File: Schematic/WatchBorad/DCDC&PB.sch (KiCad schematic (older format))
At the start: 27 parts, among them M1 Motor_DC, SW3 SW_Push, SW4 SW_Push, SW5 SW_Push, U10 TPS62740DSST, U9 MAX809S

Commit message: Fixed board's proposals. Fixed testpoints' footprint. Fixed DRC violations. Added +5V testpoint
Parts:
- TP13, TP14, TP15: footprint Measurement_Points:Measurement_Point_Round-SMD-Pad_Small -> TestPoint:TestPoint_Pad_D2.0mm
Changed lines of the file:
@@
 F 0 "TP15" H 7083 1722 50  0000 L CNN
 F 1 "TestPoint" H 7083 1677 50  0001 L CNN
-F 2 "Measurement_Points:Measurement_Point_Round-SMD-Pad_Small" H 7225 1650 50  0001 C CNN
+F 2 "TestPoint:TestPoint_Pad_D2.0mm" H 7225 1650 50  0001 C CNN
 F 3 "~" H 7225 1650 50  0001 C CNN
 	1    7025 1650
@@
 F 0 "TP14" H 2958 2572 50  0000 L CNN
 F 1 "TestPoint" H 2958 2527 50  0001 L CNN
-F 2 "Measurement_Points:Measurement_Point_Round-SMD-Pad_Small" H 3100 2500 50  0001 C CNN
+F 2 "TestPoint:TestPoint_Pad_D2.0mm" H 3100 2500 50  0001 C CNN
 F 3 "~" H 3100 2500 50  0001 C CNN
 	1    2900 2500
@@
 F 0 "TP13" H 1933 5247 50  0000 L CNN
 F 1 "TestPoint" H 1933 5202 50  0001 L CNN
-F 2 "Measurement_Points:Measurement_Point_Round-SMD-Pad_Small" H 2075 5175 50  0001 C CNN
+F 2 "TestPoint:TestPoint_Pad_D2.0mm" H 2075 5175 50  0001 C CNN
 F 3 "~" H 2075 5175 50  0001 C CNN
 	1    1875 5175

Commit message: Added new DCDC and radio antenna from Rulepas [SCHECMATIC]
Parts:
- removed U10: TPS62740DSST, Housings_SON:WSON-12-1EP_3x2mm_Pitch0.5mm, symbol WatchBorad-rescue:TPS62740DSST-DCDC_Local-WatchBorad-rescue-WatchBorad-rescue
- added C?: 100 nF, Capacitor_SMD:C_0603_1608Metric, symbol Device:C
- added C?: 10 uF, Capacitor_SMD:C_0603_1608Metric, symbol Device:C
- added C?: 4.7 pF, Capacitor_SMD:C_0603_1608Metric, symbol Device:C
- added C?: 330 pF, Capacitor_SMD:C_0603_1608Metric, symbol Device:C
- added C?: 47 pF, Capacitor_SMD:C_0603_1608Metric, symbol Device:C
- added R?: 33.2k, Resistor_SMD:R_0603_1608Metric, symbol Device:R
- added R? (x2): 200k, Resistor_SMD:R_0603_1608Metric, symbol Device:R
- added R?: 340k, Resistor_SMD:R_0603_1608Metric, symbol Device:R
- added R?: 107k, Resistor_SMD:R_0603_1608Metric, symbol Device:R
- added R?: 6.49k, Resistor_SMD:R_0603_1608Metric, symbol Device:R
- added U?: LTC3533, Housings_DFN_QFN:DFN-14-1EP_3x4mm_Pitch0.5mm, symbol WatchBorad-rescue:LTC3533-DCDC_Local
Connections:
- net labels added: COMP, DCDC_FB, L_SW_1, L_SW_2
- net labels removed: L_SW_0
- wire segments 98 -> 140
- no-connect marks 2 -> 0
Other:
- note added: "If V_OUT_MUX below 2.93V than DC/DC is off"
- note removed: "Connect this pin(5) directly \nto the output capacitor\n with a short trace"
- note removed: "If V_OUT_MUX below 3.0V than DC/DC is off"
- note removed: "LOAD(out)\nis disabled"
- moved on the sheet: C35, L1, TP15

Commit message: Added schematic files annotations [SCHEMATIC]
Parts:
- U12: renamed from U?; footprint Housings_DFN_QFN:DFN-14-1EP_3x4mm_Pitch0.5mm -> Package_DFN_QFN:DFN-14-1EP_3x4mm_P0.5mm_EP1.7x3.3mm
- gave numbers to parts that had none: 11
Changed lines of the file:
@@
 U 1 1 61909063
 P 4775 2275
-F 0 "U?" H 4775 2825 50  0000 C CNN
+AR Path="/61909063" Ref="U?"  Part="1"
+AR Path="/5F988DA5/61909063" Ref="U12"  Part="1"
+F 0 "U12" H 4775 2825 50  0000 C CNN
 F 1 "LTC3533" H 4775 2300 50  0000 C CNN
-F 2 "Housings_DFN_QFN:DFN-14-1EP_3x4mm_Pitch0.5mm" H 4775 2375 50  0001 C CNN
+F 2 "Package_DFN_QFN:DFN-14-1EP_3x4mm_P0.5mm_EP1.7x3.3mm" H 4775 2375 50  0001 C CNN
 F 3 "https://datasheet.lcsc.com/lcsc/1912111437_Analog-Devices-LTC3533EDE-TRPBF_C461524.pdf" H 4775 2375 50  0001 C CNN
 	1    4775 2275
@@
 AR Path="/5EA4867C/6191DAA1" Ref="R?"  Part="1"
 AR Path="/5F7F86D0/6191DAA1" Ref="R?"  Part="1"
-AR Path="/5F988DA5/6191DAA1" Ref="R?"  Part="1"
-F 0 "R?" H 4220 2796 50  0000 L CNN
+AR Path="/5F988DA5/6191DAA1" Ref="R3"  Part="1"
+F 0 "R3" H 4220 2796 50  0000 L CNN
 F 1 "33.2k" H 4220 2705 50  0000 L CNN
 F 2 "Resistor_SMD:R_0603_1608Metric" V 4080 2750 50  0001 C CNN
@@
 AR Path="/5EA4867C/6193FCF4" Ref="R?"  Part="1"
 AR Path="/5F7F86D0/6193FCF4" Ref="R?"  Part="1"
-AR Path="/5F988DA5/6193FCF4" Ref="R?"  Part="1"
-F 0 "R?" H 5470 2771 50  0000 L CNN
+AR Path="/5F988DA5/6193FCF4" Ref="R19"  Part="1"
+F 0 "R19" H 5470 2771 50  0000 L CNN
 F 1 "200k" H 5470 2680 50  0000 L CNN
 F 2 "Resistor_SMD:R_0603_1608Metric" V 5330 2725 50  0001 C CNN
@@
 AR Path="/5E9C1C3A/619482E5" Ref="C?"  Part="1"
 AR Path="/5F7F86D0/619482E5" Ref="C?"  Part="1"
-AR Path="/5F988DA5/619482E5" Ref="C?"  Part="1"
-F 0 "C?" H 5775 2800 50  0000 L CNN
+AR Path="/5F988DA5/619482E5" Ref="C8"  Part="1"
+F 0 "C8" H 5775 2800 50  0000 L CNN
 F 1 "100 nF" H 5775 2625 50  0000 L CNN
 F 2 "Capacitor_SMD:C_0603_1608Metric" H 5788 2575 50  0001 C CNN
@@
 AR Path="/5E9C1C3A/61961E73" Ref="C?"  Part="1"
 AR Path="/5F7F86D0/61961E73" Ref="C?"  Part="1"
-AR Path="/5F988DA5/61961E73" Ref="C?"  Part="1"
-F 0 "C?" H 7600 1975 50  0000 L CNN
+AR Path="/5F988DA5/61961E73" Ref="C40"  Part="1"
+F 0 "C40" H 7600 1975 50  0000 L CNN
 F 1 "10 uF" H 7575 1900 50  0000 L CNN
 F 2 "Capacitor_SMD:C_0603_1608Metric" H 7488 1775 50  0001 C CNN
@@
 AR Path="/5EA4867C/619772C6" Ref="R?"  Part="1"
 AR Path="/5F7F86D0/619772C6" Ref="R?"  Part="1"
-AR Path="/5F988DA5/619772C6" Ref="R?"  Part="1"
-F 0 "R?" H 6845 1971 50  0000 L CNN
+AR Path="/5F988DA5/619772C6" Ref="R25"  Part="1"
+F 0 "R25" H 6845 1971 50  0000 L CNN
 F 1 "340k" H 6845 1880 50  0000 L CNN
 F 2 "Resistor_SMD:R_0603_1608Metric" V 6705 1925 50  0001 C CNN
@@
 AR Path="/5EA4867C/6197810D" Ref="R?"  Part="1"
 AR Path="/5F7F86D0/6197810D" Ref="R?"  Part="1"
-AR Path="/5F988DA5/6197810D" Ref="R?"  Part="1"
-F 0 "R?" H 7170 2771 50  0000 L CNN
+AR Path="/5F988DA5/6197810D" Ref="R35"  Part="1"
+F 0 "R35" H 7170 2771 50  0000 L CNN
 F 1 "200k" H 7170 2680 50  0000 L CNN
 F 2 "Resistor_SMD:R_0603_1608Metric" V 7030 2725 50  0001 C CNN
@@
 AR Path="/5EA4867C/61996769" Ref="R?"  Part="1"
 AR Path="/5F7F86D0/61996769" Ref="R?"  Part="1"
-AR Path="/5F988DA5/61996769" Ref="R?"  Part="1"
-F 0 "R?" V 6325 2125 50  0000 L CNN
+AR Path="/5F988DA5/61996769" Ref="R22"  Part="1"
+F 0 "R22" V 6325 2125 50  0000 L CNN
 F 1 "107k" V 6375 2275 50  0000 L CNN
 F 2 "Resistor_SMD:R_0603_1608Metric" V 6305 2375 50  0001 C CNN
@@
 AR Path="/5E9C1C3A/619CAFA1" Ref="C?"  Part="1"
 AR Path="/5F7F86D0/619CAFA1" Ref="C?"  Part="1"
-AR Path="/5F988DA5/619CAFA1" Ref="C?"  Part="1"
-F 0 "C?" V 6325 2375 50  0000 L CNN
+AR Path="/5F988DA5/619CAFA1" Ref="C11"  Part="1"
+F 0 "C11" V 6325 2375 50  0000 L CNN
 F 1 "4.7 pF" V 6500 2475 50  0000 L CNN
 F 2 "Capacitor_SMD:C_0603_1608Metric" H 6413 2450 50  0001 C CNN
@@
 AR Path="/5E9C1C3A/619CBCE2" Ref="C?"  Part="1"
 AR Path="/5F7F86D0/619CBCE2" Ref="C?"  Part="1"
-AR Path="/5F988DA5/619CBCE2" Ref="C?"  Part="1"
-F 0 "C?" V 6775 2150 50  0000 L CNN
+AR Path="/5F988DA5/619CBCE2" Ref="C17"  Part="1"
+F 0 "C17" V 6775 2150 50  0000 L CNN
 F 1 "330 pF" V 6950 2250 50  0000 L CNN
 F 2 "Capacitor_SMD:C_0603_1608Metric" H 6863 2225 50  0001 C CNN
@@
 AR Path="/5EA4867C/619E85E1" Ref="R?"  Part="1"
 AR Path="/5F7F86D0/619E85E1" Ref="R?"  Part="1"
-AR Path="/5F988DA5/619E85E1" Ref="R?"  Part="1"
-F 0 "R?" H 7170 1971 50  0000 L CNN
+AR Path="/5F988DA5/619E85E1" Ref="R34"  Part="1"
+F 0 "R34" H 7170 1971 50  0000 L CNN
 F 1 "6.49k" H 7170 1880 50  0000 L CNN
 F 2 "Resistor_SMD:R_0603_1608Metric" V 7030 1925 50  0001 C CNN
@@
 AR Path="/5E9C1C3A/619ED8AC" Ref="C?"  Part="1"
 AR Path="/5F7F86D0/619ED8AC" Ref="C?"  Part="1"
-AR Path="/5F988DA5/619ED8AC" Ref="C?"  Part="1"
-F 0 "C?" V 6900 2400 50  0000 L CNN
+AR Path="/5F988DA5/619ED8AC" Ref="C39"  Part="1"
+F 0 "C39" V 6900 2400 50  0000 L CNN
 F 1 "47 pF" V 7000 2400 50  0000 L CNN
 F 2 "Capacitor_SMD:C_0603_1608Metric" H 6988 2025 50  0001 C CNN

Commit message: Added LDO instead of DC-DC. Added board routing accroding to the new peripheral changes [SCHEMATIC]
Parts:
- removed C11: 4.7 pF, Capacitor_SMD:C_0603_1608Metric, symbol Device:C
- removed C17: 330 pF, Capacitor_SMD:C_0603_1608Metric, symbol Device:C
- removed C35: 10 uF, Capacitor_SMD:C_0603_1608Metric, symbol Device:C
- removed C39: 47 pF, Capacitor_SMD:C_0603_1608Metric, symbol Device:C
- removed C8: 100 nF, Capacitor_SMD:C_0603_1608Metric, symbol Device:C
- removed L1: 2.2 uH 13.75 mOHM 1.2 A, Inductors_SMD:L_0805_HandSoldering, symbol pspice:INDUCTOR
- removed R22: 107k, Resistor_SMD:R_0603_1608Metric, symbol Device:R
- removed R25: 340k, Resistor_SMD:R_0603_1608Metric, symbol Device:R
- removed R34: 6.49k, Resistor_SMD:R_0603_1608Metric, symbol Device:R
- removed R35: 200k, Resistor_SMD:R_0603_1608Metric, symbol Device:R
- removed U12: LTC3533, Package_DFN_QFN:DFN-14-1EP_3x4mm_P0.5mm_EP1.7x3.3mm, symbol WatchBorad-rescue:LTC3533-DCDC_Local
- added U12: TPS73501DRBR, TPS73501DRBR:TPS73501DRBR, symbol TPS73501DRBR:TPS73501DRBR
- R19: value 200k -> 220
- R3: value 33.2k -> 330
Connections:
- net labels added: LDO_RDIV
- net labels removed: COMP, DCDC_FB, L_SW_1, L_SW_2
- wire segments 140 -> 89
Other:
- note added: "LDO 3.0V\n\n"
- note added: "Vout = 3.0V\n"
- note added: "Vout=(R1+R2)/R2 * 1.208\n"
- note removed: "DCDC converter 3.3V\n\n"
- note removed: "Vout = 3.3V\n"
- moved on the sheet: C40, TP15

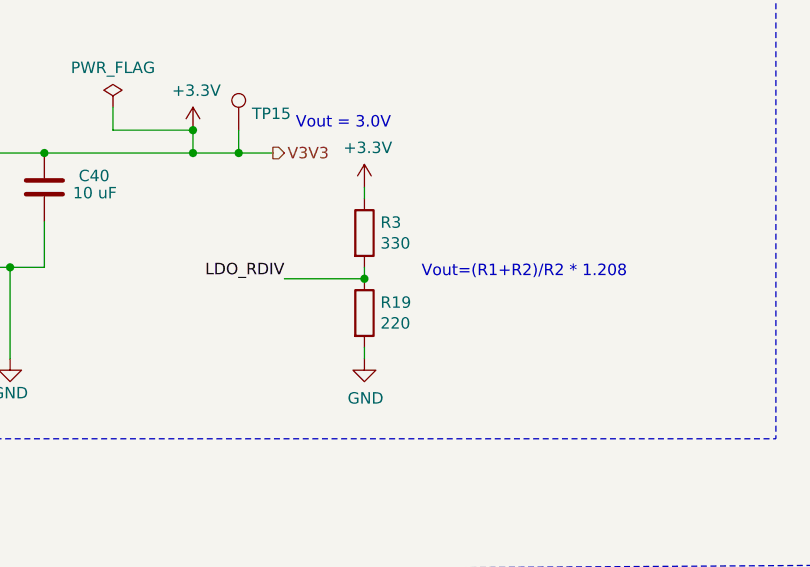
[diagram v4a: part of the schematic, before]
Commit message: Adjusted LDO resisors [SCHEMATIC]
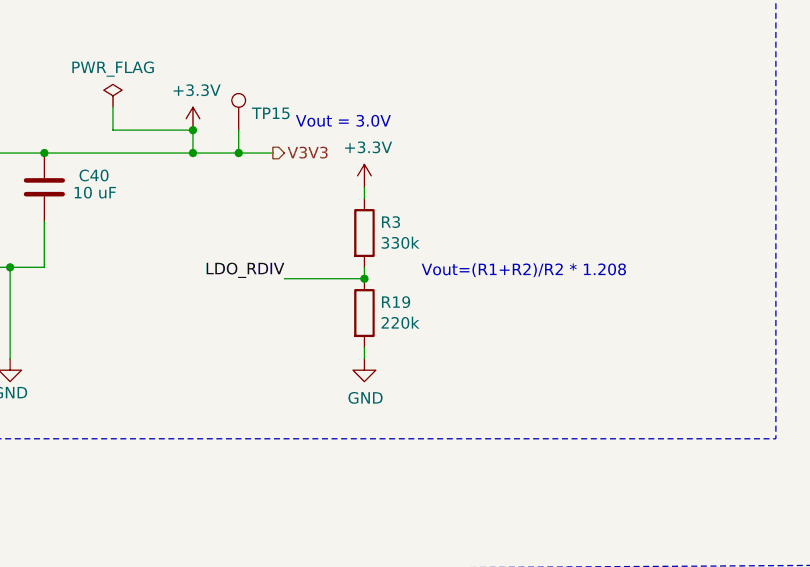
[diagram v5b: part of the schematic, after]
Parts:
- R19: value 220 -> 220k
- R3: value 330 -> 330k
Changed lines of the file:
@@
 P 7300 2800
 F 0 "R19" H 7370 2846 50  0000 L CNN
-F 1 "220" H 7370 2755 50  0000 L CNN
+F 1 "220k" H 7370 2755 50  0000 L CNN
 F 2 "Resistor_SMD:R_0603_1608Metric" V 7230 2800 50  0001 C CNN
 F 3 "~" H 7300 2800 50  0001 C CNN
@@
 P 7300 2450
 F 0 "R3" H 7370 2496 50  0000 L CNN
-F 1 "330" H 7370 2405 50  0000 L CNN
+F 1 "330k" H 7370 2405 50  0000 L CNN
 F 2 "Resistor_SMD:R_0603_1608Metric" V 7230 2450 50  0001 C CNN
 F 3 "~" H 7300 2450 50  0001 C CNN

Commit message: Added missed components to the symbol lists [SCHEMATIC]
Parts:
- C32, C34, C36, C37, C38: lcsc (none) -> https://lcsc.com/product-detail/Multilayer-Ceramic-Capacito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
- M1: lcsc (none) -> https://www.aliexpress.com/item/32844746278.html?spm=a2g0o.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
- U12: lcsc (none) -> https://lcsc.com/product-detail/Linear-Voltage-Regulators-L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
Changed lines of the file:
@@
 F 2 "Capacitor_SMD:C_0603_1608Metric" H 2038 2350 50  0001 C CNN
 F 3 "~" H 2000 2500 50  0001 C CNN
+F 4 "https://lcsc.com/product-detail/Multilayer-Ceramic-Capacitors-MLCC-SMD-SMT_YAGEO-CC0603KRX7R9BB104_C14663.html" H 2000 2500 50  0001 C CNN "lcsc"
 	1    2000 2500
 	1    0    0    -1
@@
 F 2 "LocalFootprints:VibrationMorot4x4x11" H 2975 4460 50  0001 C CNN
 F 3 "https://www.aliexpress.com/item/32844746278.html?spm=a2g0o.productlist.0.0.24ef228a6Cfn5S&algo_pvid=3165a7c1-ba73-4c2c-bb27-6dacea1bed25&algo_expid=3165a7c1-ba73-4c2c-bb27-6dacea1bed25-0&btsid=0b8b15c915866028623212205ec781&ws_ab_test=searchweb0_0,searchweb201602_,searchweb201603_" H 2975 4460 50  0001 C CNN
+F 4 "https://www.aliexpress.com/item/32844746278.html?spm=a2g0o.productlist.0.0.24ef228a6Cfn5S&algo_pvid=3165a7c1-ba73-4c2c-bb27-6dacea1bed25&algo_expid=3165a7c1-ba73-4c2c-bb27-6dacea1bed25-0&btsid=0b8b15c915866028623212205ec781&ws_ab_test=searchweb0_0,searchweb201602_,searchweb201603_" H 2975 4550 50  0001 C CNN "lcsc"
 	1    2975 4550
 	1    0    0    -1
@@
 F 2 "Capacitor_SMD:C_0603_1608Metric" H 3438 4475 50  0001 C CNN
 F 3 "~" H 3400 4625 50  0001 C CNN
+F 4 "https://lcsc.com/product-detail/Multilayer-Ceramic-Capacitors-MLCC-SMD-SMT_Samsung-Electro-Mechanics-CL10B104KO8NNNC_C66501.html" H 3400 4625 50  0001 C CNN "lcsc"
 	1    3400 4625
 	1    0    0    -1
@@
 F 2 "Capacitor_SMD:C_0603_1608Metric" H 7763 5350 50  0001 C CNN
 F 3 "~" H 7725 5500 50  0001 C CNN
+F 4 "https://lcsc.com/product-detail/Multilayer-Ceramic-Capacitors-MLCC-SMD-SMT_YAGEO-CC0603KRX7R9BB104_C14663.html" H 7725 5500 50  0001 C CNN "lcsc"
 	1    7725 5500
 	1    0    0    -1
@@
 F 2 "Capacitor_SMD:C_0603_1608Metric" H 8463 5350 50  0001 C CNN
 F 3 "~" H 8425 5500 50  0001 C CNN
+F 4 "https://lcsc.com/product-detail/Multilayer-Ceramic-Capacitors-MLCC-SMD-SMT_YAGEO-CC0603KRX7R9BB104_C14663.html" H 8425 5500 50  0001 C CNN "lcsc"
 	1    8425 5500
 	1    0    0    -1
@@
 F 2 "Capacitor_SMD:C_0603_1608Metric" H 9188 5350 50  0001 C CNN
 F 3 "~" H 9150 5500 50  0001 C CNN
+F 4 "https://lcsc.com/product-detail/Multilayer-Ceramic-Capacitors-MLCC-SMD-SMT_YAGEO-CC0603KRX7R9BB104_C14663.html" H 9150 5500 50  0001 C CNN "lcsc"
 	1    9150 5500
 	1    0    0    -1
@@
 F 2 "TPS73501DRBR:TPS73501DRBR" H 4950 2400 50  0001 L BNN
 F 3 "" H 4950 2400 50  0001 L BNN
+F 4 "https://lcsc.com/product-detail/Linear-Voltage-Regulators-LDO_Texas-Instruments-TPS73501DRBR_C130077.html" H 4950 2400 50  0001 C CNN "lcsc"
 	1    4950 2400
 	1    0    0    -1

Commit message: Added missed resistors to the lcsc [SCHEMATIC][BOM]
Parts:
- R19, R26, R27, R28, R29, R3, R30, R31, R32, R33: lcsc (none) -> https://www.lcsc.com/product-detail/Chip-Resistor-Surface-M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
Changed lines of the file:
@@
 F 2 "Resistor_SMD:R_0603_1608Metric" V 7905 5500 50  0001 C CNN
 F 3 "~" H 7975 5500 50  0001 C CNN
+F 4 "https://www.lcsc.com/product-detail/Chip-Resistor-Surface-Mount_YAGEO-RC0603FR-0710KL_C98220.html" H 7975 5500 50  0001 C CNN "lcsc"
 	1    7975 5500
 	1    0    0    -1
@@
 F 2 "Resistor_SMD:R_0603_1608Metric" V 8605 5500 50  0001 C CNN
 F 3 "~" H 8675 5500 50  0001 C CNN
+F 4 "https://www.lcsc.com/product-detail/Chip-Resistor-Surface-Mount_YAGEO-RC0603FR-0710KL_C98220.html" H 8675 5500 50  0001 C CNN "lcsc"
 	1    8675 5500
 	1    0    0    -1
@@
 F 2 "Resistor_SMD:R_0603_1608Metric" V 9330 5500 50  0001 C CNN
 F 3 "~" H 9400 5500 50  0001 C CNN
+F 4 "https://www.lcsc.com/product-detail/Chip-Resistor-Surface-Mount_YAGEO-RC0603FR-0710KL_C98220.html" H 9400 5500 50  0001 C CNN "lcsc"
 	1    9400 5500
 	1    0    0    -1
@@
 F 2 "Resistor_SMD:R_0603_1608Metric" V 2605 5500 50  0001 C CNN
 F 3 "~" H 2675 5500 50  0001 C CNN
+F 4 "https://www.lcsc.com/product-detail/Chip-Resistor-Surface-Mount_YAGEO-RC0603FR-0710KL_C98220.html" H 2675 5500 50  0001 C CNN "lcsc"
 	1    2675 5500
 	1    0    0    -1
@@
 F 2 "Resistor_SMD:R_0603_1608Metric" V 2330 5175 50  0001 C CNN
 F 3 "https://lcsc.com/product-detail/Others_Viking-Tech-ARG03FTC3300_C217969.html" H 2400 5175 50  0001 C CNN
+F 4 "https://www.lcsc.com/product-detail/Chip-Resistor-Surface-Mount_Walsin-Tech-Corp-WR06X331JTL_C384242.html" H 2400 5175 50  0001 C CNN "lcsc"
 	1    2400 5175
 	0    1    1    0
@@
 F 2 "Resistor_SMD:R_0603_1608Metric" V 7030 5050 50  0001 C CNN
 F 3 "https://lcsc.com/product-detail/Others_Viking-Tech-ARG03FTC3300_C217969.html" H 7100 5050 50  0001 C CNN
+F 4 "https://www.lcsc.com/product-detail/Chip-Resistor-Surface-Mount_Walsin-Tech-Corp-WR06X331JTL_C384242.html" H 7100 5050 50  0001 C CNN "lcsc"
 	1    7100 5050
 	0    1    1    0
@@
 F 2 "Resistor_SMD:R_0603_1608Metric" V 7030 5150 50  0001 C CNN
 F 3 "https://lcsc.com/product-detail/Others_Viking-Tech-ARG03FTC3300_C217969.html" H 7100 5150 50  0001 C CNN
+F 4 "https://www.lcsc.com/product-detail/Chip-Resistor-Surface-Mount_Walsin-Tech-Corp-WR06X331JTL_C384242.html" H 7100 5150 50  0001 C CNN "lcsc"
 	1    7100 5150
 	0    1    1    0
@@
 F 2 "Resistor_SMD:R_0603_1608Metric" V 7030 5250 50  0001 C CNN
 F 3 "https://lcsc.com/product-detail/Others_Viking-Tech-ARG03FTC3300_C217969.html" H 7100 5250 50  0001 C CNN
+F 4 "https://www.lcsc.com/product-detail/Chip-Resistor-Surface-Mount_Walsin-Tech-Corp-WR06X331JTL_C384242.html" H 7100 5250 50  0001 C CNN "lcsc"
 	1    7100 5250
 	0    1    1    0
@@
 F 2 "Resistor_SMD:R_0603_1608Metric" V 7230 2800 50  0001 C CNN
 F 3 "~" H 7300 2800 50  0001 C CNN
+F 4 "https://www.lcsc.com/product-detail/Chip-Resistor-Surface-Mount_FH-Guangdong-Fenghua-Advanced-Tech-RS-03K224JT_C118377.html" H 7300 2800 50  0001 C CNN "lcsc"
 	1    7300 2800
 	1    0    0    -1
@@
 F 2 "Resistor_SMD:R_0603_1608Metric" V 7230 2450 50  0001 C CNN
 F 3 "~" H 7300 2450 50  0001 C CNN
+F 4 "https://www.lcsc.com/product-detail/Chip-Resistor-Surface-Mount_Resistor-Today-AECR0603F330KK9_C328354.html" H 7300 2450 50  0001 C CNN "lcsc"
 	1    7300 2450
 	1    0    0    -1
